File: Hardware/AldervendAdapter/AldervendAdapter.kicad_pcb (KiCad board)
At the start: 2 copper layers, 85 x 60 mm, 7 parts, among them J101 MDB_IN, J102 MDB_OUT, U101 ESP32-WROOM-32D

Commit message: Add aldervon logo
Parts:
- added G***: LOGO, Aldervon:Aldervon_logo, F.Cu at (174.0, 121.0)

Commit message: Add 3d
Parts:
- moved J101 1.00 mm to (210.7, 87.6)
- moved J102 1.00 mm to (210.7, 103.6)
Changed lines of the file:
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@@
 		)
 		(embedded_fonts no)
-		(model "${KICAD9_3DMODEL_DIR}/RF_Module.3dshapes/ESP32-WROOM-32D.step"
+		(model "${KICAD9_3DMODEL_DIR}/RF_Module.3dshapes/ESP32-WROOM-32E.wrl"
 			(offset
-				(xyz 0 0 0)
+				(xyz 0 3 0)
 			)
 			(scale
@@
 			)
 			(rotate
-				(xyz 0 0 0)
+				(xyz -0 -0 -0)
 			)
 		)
@@
 	(footprint "Connector_Molex:Molex_Mini-Fit_Jr_5569-06A2_2x03_P4.20mm_Horizontal"
 		(layer "F.Cu")
-		(at 209.7 87.6 -90)
+		(at 210.7 87.6 -90)
 		(descr "Molex Mini-Fit Jr. Power Connectors, old mpn/engineering number: 5569-06A2, example for new mpn: 39-30-0060, 3 Pins per row, Mounting: Snap-in Plastic Peg PCB Lock (http://www.molex.com/pdm_docs/sd/039300020_sd.pdf), generated with kicad-footprint-generator")
 		(tags "connector Molex Mini-Fit_Jr horizontalplastic_peg")
@@
 		)
 		(embedded_fonts no)
-		(model "${KICAD9_3DMODEL_DIR}/Connector_Molex.3dshapes/Molex_Mini-Fit_Jr_5569-06A2_2x03_P4.20mm_Horizontal.step"
+		(model "${KIPRJMOD}/Libraries/Aldervon-Libs/3d/Molex Jr-Body.step"
 			(offset
-				(xyz 0 0 0)
+				(xyz 4.25 7.5 0)
 			)
 			(scale
@@
 			)
 			(rotate
-				(xyz 0 0 0)
+				(xyz -0 -0 -0)
 			)
 		)
@@
 	(footprint "Connector_Molex:Molex_Mini-Fit_Jr_5569-06A2_2x03_P4.20mm_Horizontal"
 		(layer "F.Cu")
-		(at 209.7 103.605 -90)
+		(at 210.7 103.605 -90)
 		(descr "Molex Mini-Fit Jr. Power Connectors, old mpn/engineering number: 5569-06A2, example for new mpn: 39-30-0060, 3 Pins per row, Mounting: Snap-in Plastic Peg PCB Lock (http://www.molex.com/pdm_docs/sd/039300020_sd.pdf), generated with kicad-footprint-generator")
 		(tags "connector Molex Mini-Fit_Jr horizontalplastic_peg")
@@
 		)
 		(embedded_fonts no)
-		(model "${KICAD9_3DMODEL_DIR}/Connector_Molex.3dshapes/Molex_Mini-Fit_Jr_5569-06A2_2x03_P4.20mm_Horizontal.step"
+		(model "${KIPRJMOD}/Libraries/Aldervon-Libs/3d/Molex Jr-Body.step"
 			(offset
-				(xyz 0 0 0)
+				(xyz 4.25 7.5 0)
 			)
 			(scale
@@
 			)
 			(rotate
-				(xyz 0 0 0)
-			)
-		)
+				(xyz -0 -0 -0)
+			)
+		)

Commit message: Enough free work for today
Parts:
- added C101: 680uF, Capacitor_SMD:C_Elec_10x10.2, F.Cu at (170.5, 96.0)
- added C102: 220uF, Capacitor_SMD:C_Elec_6.3x5.4, F.Cu at (184.0, 78.0)
- added D101: SS34, Diode_SMD:D_SMA, F.Cu at (163.7, 107.5)
- added L101: L, Inductor_SMD:L_6.3x6.3_H3, F.Cu at (183.3, 86.0)
- added Q101: 2N3904, Package_TO_SOT_SMD:SOT-323_SC-70, F.Cu at (160.8, 99.1)
- added R101: R_Small, Resistor_SMD:R_0805_2012Metric, F.Cu at (160.7, 89.8)
- added R102: 1k, Resistor_SMD:R_0805_2012Metric, F.Cu at (160.7, 92.8)
- added R103: 0R, Resistor_SMD:R_0805_2012Metric, F.Cu at (160.7, 95.7)
- added U102: TLP2310, Package_SO:SO-5-6_4.55x3.7mm_P1.27mm, F.Cu at (168.6, 108.0)
- added U103: ESP32-C6-MINI-1, RF_Module:ESP32-C6-MINI-1, F.Cu at (151.4, 99.8)
- added U104: LM2596S-5, Package_TO_SOT_SMD:TO-263-5_TabPin3, F.Cu at (170.2, 81.5)
- J101: value MDB_IN -> MDB_PUBLISHER
- J102: value MDB_OUT -> MDB_SUBSCRIBER
- U101: value ESP32-WROOM-32D -> TLP2310; footprint RF_Module:ESP32-WROOM-32D -> Package_SO:SO-5-6_4.55x3.7mm_P1.27mm
- moved U101 19.6 mm to (173.8, 108.0), turned to -90 degrees
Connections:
- J101 pad 1: unconnected-(J101-Pin_1-Pad1) -> +24V
- J101 pad 2: unconnected-(J101-Pin_2-Pad2) -> GND
- J101 pad 4: unconnected-(J101-Pin_4-Pad4) -> /MDB_RXD
- J101 pad 5: unconnected-(J101-Pin_5-Pad5) -> /MDB_TXD
- J101 pad 6: unconnected-(J101-Pin_6-Pad6) -> GND
- J102 pad 1: unconnected-(J102-Pin_1-Pad1) -> +24V
- J102 pad 2: unconnected-(J102-Pin_2-Pad2) -> GND
- J102 pad 4: unconnected-(J102-Pin_4-Pad4) -> /MDB_RXD
- J102 pad 5: unconnected-(J102-Pin_5-Pad5) -> /MDB_TXD
- J102 pad 6: unconnected-(J102-Pin_6-Pad6) -> GND
- U101 pad 1: Net-(U101-GND-Pad1) -> unconnected-(U101-A-Pad1)

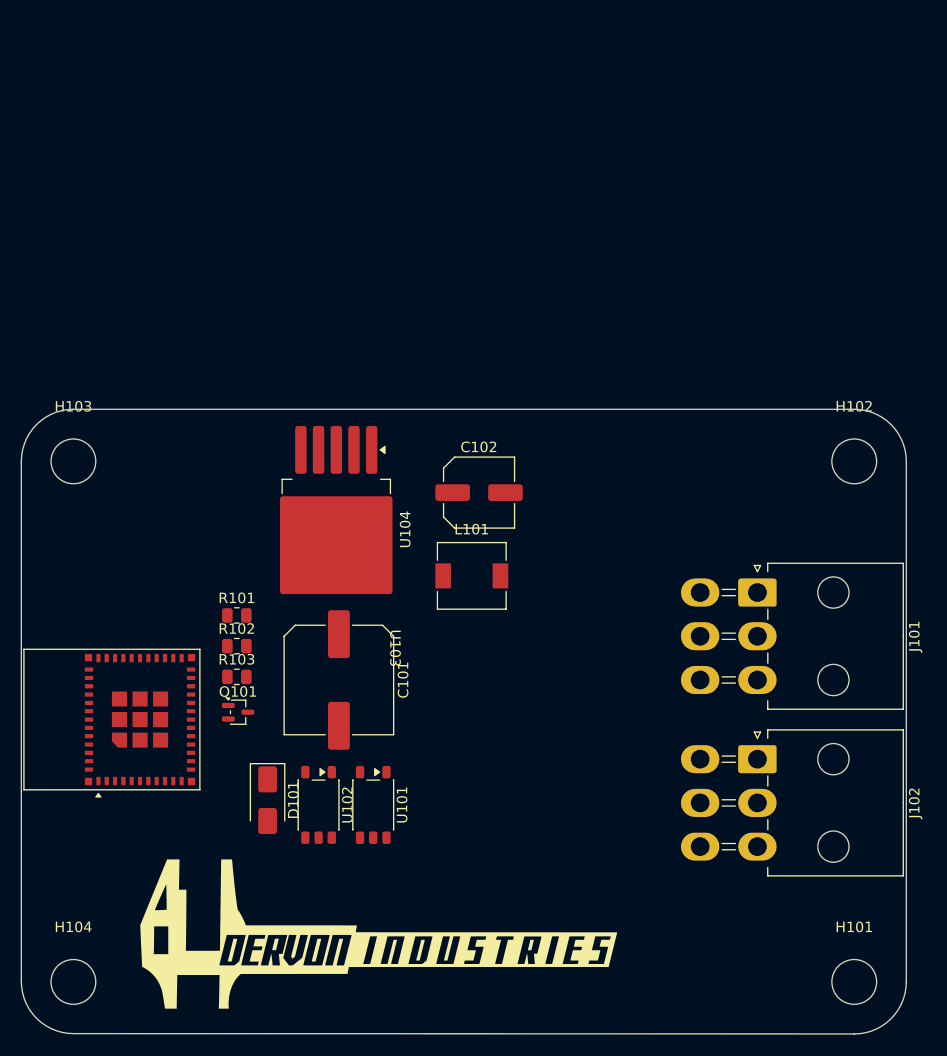
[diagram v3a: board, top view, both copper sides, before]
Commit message: Finish schematic
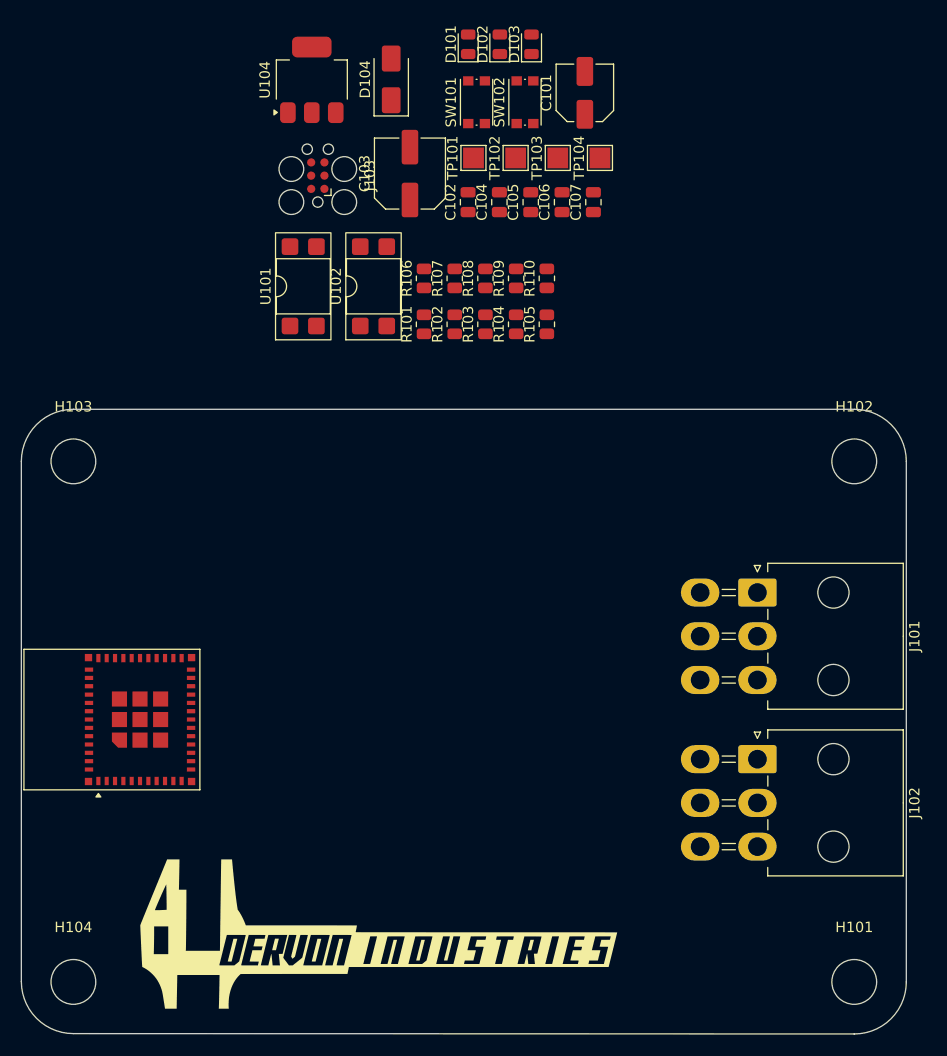
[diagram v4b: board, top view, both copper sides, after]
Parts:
- removed L101: L, Inductor_SMD:L_6.3x6.3_H3
- removed Q101: 2N3904, Package_TO_SOT_SMD:SOT-323_SC-70
- added C103: 22uF, Capacitor_SMD:C_Elec_6.3x5.4, F.Cu at (177.3, 47.4)
- added C104: 10uF, Capacitor_SMD:C_0805_2012Metric, F.Cu at (185.9, 50.1)
- added C105: 100nF, Capacitor_SMD:C_0805_2012Metric, F.Cu at (188.9, 50.1)
- added C106: 100nF, Capacitor_SMD:C_0805_2012Metric, F.Cu at (191.9, 50.1)
- added C107: 100nF, Capacitor_SMD:C_0805_2012Metric, F.Cu at (194.9, 50.1)
- added D102: 3.3V Power, LED_SMD:LED_0805_2012Metric, F.Cu at (186.0, 34.9)
- added D103: 3.3V Power, LED_SMD:LED_0805_2012Metric, F.Cu at (189.0, 34.9)
- added D104: SS14, Diode_SMD:D_SMA, F.Cu at (175.5, 38.3)
- added J103: PROG, Connector:Tag-Connect_TC2030-IDC-FP_2x03_P1.27mm_Vertical, F.Cu at (168.5, 47.6)
- added R104: 0R, Resistor_SMD:R_0805_2012Metric, F.Cu at (187.5, 61.8)
- added R105: 330R, Resistor_SMD:R_0805_2012Metric, F.Cu at (190.5, 61.8)
- added R106: 330R, Resistor_SMD:R_0805_2012Metric, F.Cu at (178.7, 57.4)
- added R107: 5.1k, Resistor_SMD:R_0805_2012Metric, F.Cu at (181.6, 57.4)
- added R108: 5.1k, Resistor_SMD:R_0805_2012Metric, F.Cu at (184.6, 57.4)
- added R109: 270R, Resistor_SMD:R_0805_2012Metric, F.Cu at (187.5, 57.4)
- added R110: 680R, Resistor_SMD:R_0805_2012Metric, F.Cu at (190.5, 57.4)
- added SW101: RESET, Button_Switch_SMD:SW_Push_1P1T_NO_CK_KMR2, F.Cu at (183.7, 40.5)
- added SW102: BOOT, Button_Switch_SMD:SW_Push_1P1T_NO_CK_KMR2, F.Cu at (188.4, 40.5)
- added TP101: TestPoint, TestPoint:TestPoint_Pad_2.0x2.0mm, F.Cu at (183.4, 45.9)
- added TP102: TestPoint, TestPoint:TestPoint_Pad_2.0x2.0mm, F.Cu at (187.5, 45.9)
- added TP103: TestPoint, TestPoint:TestPoint_Pad_2.0x2.0mm, F.Cu at (191.5, 45.9)
- added TP104: TestPoint, TestPoint:TestPoint_Pad_2.0x2.0mm, F.Cu at (195.6, 45.9)
- C101: value 680uF -> 33uF; footprint Capacitor_SMD:C_Elec_10x10.2 -> Capacitor_SMD:C_Elec_5x5.4
- C102: value 220uF -> 10uF; footprint Capacitor_SMD:C_Elec_6.3x5.4 -> Capacitor_SMD:C_0805_2012Metric
- D101: value SS34 -> 5V Power; footprint Diode_SMD:D_SMA -> LED_SMD:LED_0805_2012Metric
- J101: value MDB_PUBLISHER -> MDB_MASTER
- J102: value MDB_SUBSCRIBER -> MDB_SLAVE
- R101: value R_Small -> 10k
- R102: value 1k -> 270R
- R103: value 0R -> ?
- U101, U102: value TLP2310 -> PC817; footprint Package_SO:SO-5-6_4.55x3.7mm_P1.27mm -> Package_DIP:DIP-4_W7.62mm_SMDSocket_SmallPads
- U104: value LM2596S-5 -> AMS1117-3.3; footprint Package_TO_SOT_SMD:TO-263-5_TabPin3 -> Package_TO_SOT_SMD:SOT-223-3_TabPin2
- moved D101 75.1 mm to (182.9, 34.9), turned to 90 degrees
- moved C101 61.1 mm to (194.1, 39.6), turned to 90 degrees
- moved U101 50.3 mm to (167.1, 58.2), turned to 90 degrees
- moved U102 50.1 mm to (173.8, 58.2), turned to 90 degrees
- moved U104 43.3 mm to (167.9, 38.4), turned to 90 degrees
- moved R103 41.4 mm to (184.6, 61.8), turned to 90 degrees
- moved R102 37.3 mm to (181.6, 61.8), turned to 90 degrees
- moved R101 33.2 mm to (178.7, 61.8), turned to 90 degrees
- moved C102 27.9 mm to (182.9, 50.1), turned to 90 degrees
- renumbered U103 to U106
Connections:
- C101 pad 1: +24V -> +36V
- C101 pad 2: GND -> Earth
- C102 pad 1: Net-(U104-FB) -> +36V
- C102 pad 2: GND -> Earth
- D101 pad 1: Net-(D101-K) -> GND
- D101 pad 2: GND -> Net-(D101-A)
- J101 pad 1: +24V -> +36V
- J101 pad 2: GND -> Earth
- J101 pad 6: GND -> Earth
- J102 pad 1: +24V -> +36V
- J102 pad 2: GND -> Earth
- J102 pad 6: GND -> Earth
- R101 pad 1: unconnected-(R101-Pad1) -> /UART_RX
- R101 pad 2: unconnected-(R101-Pad2) -> +3.3V
- R102 pad 1: unconnected-(R102-Pad1) -> Net-(R102-Pad1)
- R102 pad 2: GND -> /UART_TX
- R103 pad 1: Net-(U104-~{ON}/OFF) -> +3.3V
- R103 pad 2: GND -> /MDB_RXD
- U101 pad 1: unconnected-(U101-A-Pad1) -> Net-(R102-Pad1)
- U101 pad 3: unconnected-(U101-K-Pad3) -> Earth
- U101 pad 4: unconnected-(U101-GND-Pad4) -> /MDB_RXD
- U102 pad 1: unconnected-(U102-A-Pad1) -> Net-(R105-Pad1)
- U102 pad 3: unconnected-(U102-K-Pad3) -> GND
- U102 pad 4: unconnected-(U102-GND-Pad4) -> /UART_RX
- U104 pad 1: +24V -> GND
- U104 pad 2: Net-(D101-K) -> +3.3V
- U104 pad 3: GND -> +5V
- U106 pad 12: unconnected-(U103-IO0-Pad12) -> Net-(U106-IO0)
- U106 pad 13: unconnected-(U103-IO1-Pad13) -> Net-(U106-IO1)
- U106 pad 16: unconnected-(U103-IO7-Pad16) -> Net-(U106-IO7)
- U106 pad 17: unconnected-(U103-IO12-Pad17) -> /D-
- U106 pad 18: unconnected-(U103-IO13-Pad18) -> /D+
- U106 pad 22: unconnected-(U103-IO8-Pad22) -> Net-(U106-IO8)
- U106 pad 23: unconnected-(U103-IO9-Pad23) -> /BOOT
- U106 pad 30: unconnected-(U103-RXD0-Pad30) -> /UART_RX
- U106 pad 31: unconnected-(U103-TXD0-Pad31) -> /UART_TX
- U106 pad 5: unconnected-(U103-IO2-Pad5) -> /STAT
- U106 pad 8: unconnected-(U103-EN-Pad8) -> /RESET

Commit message: Add all but finishing touches
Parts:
- added U103: K7805M-1000R3, Aldervon:K7805M-1000R3, F.Cu at (209.5, 77.5)
- D103: value 3.3V Power -> Stat
- J103: moved to B.Cu
- moved D103 90.2 mm to (157.5, 119.4)
- moved SW101 80.4 mm to (148.0, 112.5)
- moved C105 78.1 mm to (147.9, 116.5), turned to 180 degrees
- moved C107 73.0 mm to (150.5, 108.0), turned to 0 degrees
- moved R107 70.3 mm to (149.5, 120.0), turned to 0 degrees
- moved TP101 70.1 mm to (169.0, 114.5)
- moved TP102 68.2 mm to (169.0, 111.5)
- moved R110 66.7 mm to (157.5, 115.4)
- moved TP103 66.6 mm to (169.0, 108.5)
- moved D104 62.4 mm to (170.5, 100.5), turned to 180 degrees
- moved SW102 61.2 mm to (150.3, 88.4), turned to 180 degrees
- moved TP104 57.3 mm to (163.0, 93.0)
- moved J103 52.9 mm to (162.2, 100.1), turned to 180 degrees
- moved R108 43.3 mm to (154.3, 88.4)
- moved D102 43.2 mm to (176.0, 77.0), turned to -90 degrees
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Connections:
- D101 pad 1: GND -> Earth
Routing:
- net +3.3V: track 0.00 -> 131.0 mm, vias 0 -> 5
- net +5V: track 0.00 -> 69.4 mm, vias 0 -> 2
- net /UART_RX: track 0.00 -> 41.7 mm
- net /MDB_RXD: track 0.00 -> 40.9 mm, vias 0 -> 2
- net +36V: track 0.00 -> 37.6 mm
- net /UART_TX: track 0.00 -> 34.4 mm
- net /MDB_TXD: track 0.00 -> 23.0 mm
- net /RESET: track 0.00 -> 17.6 mm, vias 0 -> 2
- net Net-(U106-IO0): track 0.00 -> 16.8 mm
- net /BOOT: track 0.00 -> 16.6 mm, vias 0 -> 2
- net Net-(U106-IO1): track 0.00 -> 15.9 mm
- net Net-(U106-IO7): track 0.00 -> 15.6 mm
- net /D+: track 0.00 -> 12.8 mm, vias 0 -> 1
- net /D-: track 0.00 -> 12.5 mm, vias 0 -> 1
- net /STAT: track 0.00 -> 12.3 mm
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- added copper zone on B.Cu, net Earth
- added copper zone on F.Cu, net Earth
- added copper zone on B.Cu, net GND
- added copper zone on F.Cu, net GND
